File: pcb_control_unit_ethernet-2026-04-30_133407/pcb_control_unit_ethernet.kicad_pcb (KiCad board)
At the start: 4 copper layers, 188 x 65 mm, 274 parts, among them J1 STDC14, J17 STEP1, J18 STEP2, J2 Micro_SD_Card_Det1, J23 Weight, J3 INB, J30 Valve, J4 DC IN, J5 USB STM32, J6 USB STM32, Q1 IRLML6344, Q2 IRLML6344, Q3 IRLML6344, Q4 MMBT4403, Q5 IRLML6344, Q6 IRLML6344, SW1 Reset, SW2 Boot, U1 STM32H563VITx, U10 SIT3051TK, U11 74AHCT125, U12 TPS54202DDC, U16 24LC512, U2 LAN8742A, U4 TPS54202DDC, U5 AMS1117-3.3, U6 INA226, U7 TMC2209, U8 TMC2209, U9 HX711, X1 MT3608, Y1 25MHz, Y2 25MHz

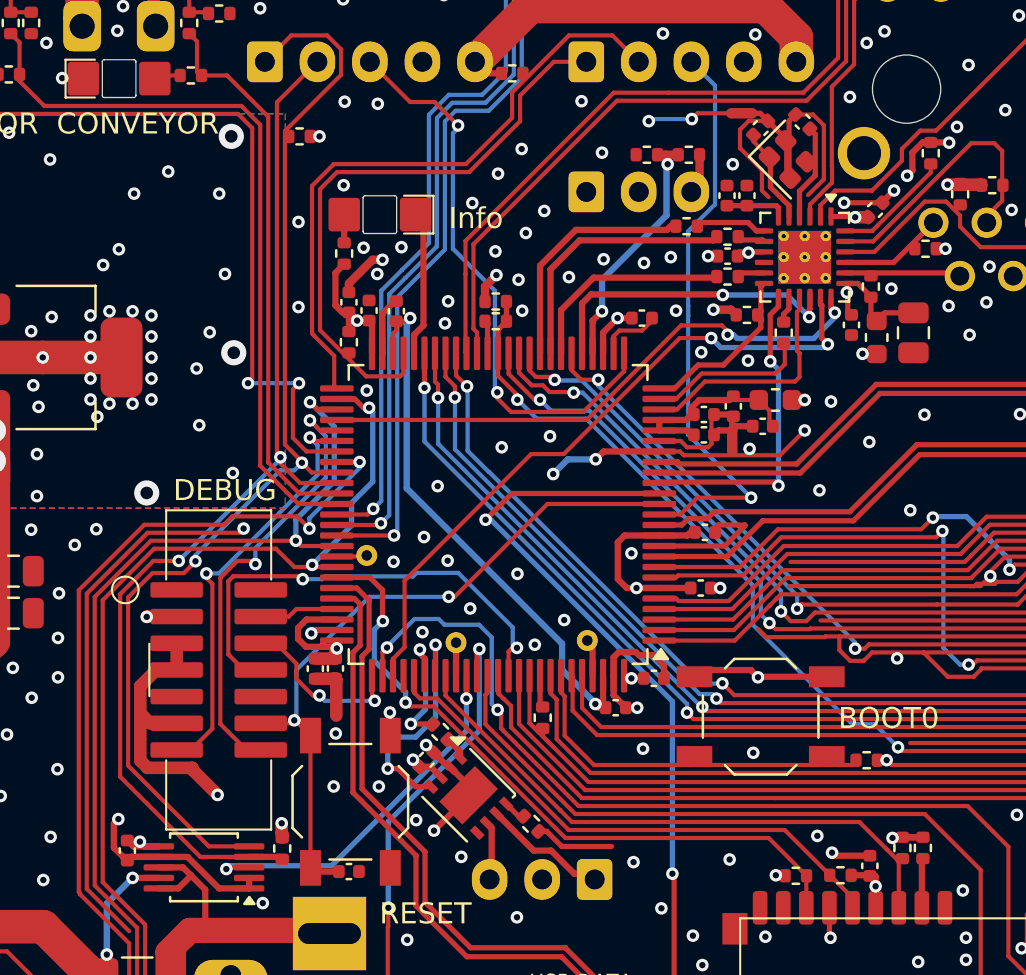
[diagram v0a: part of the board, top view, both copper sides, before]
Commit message: pcb_control_unit_ethercat as ordered @ JLCPCB
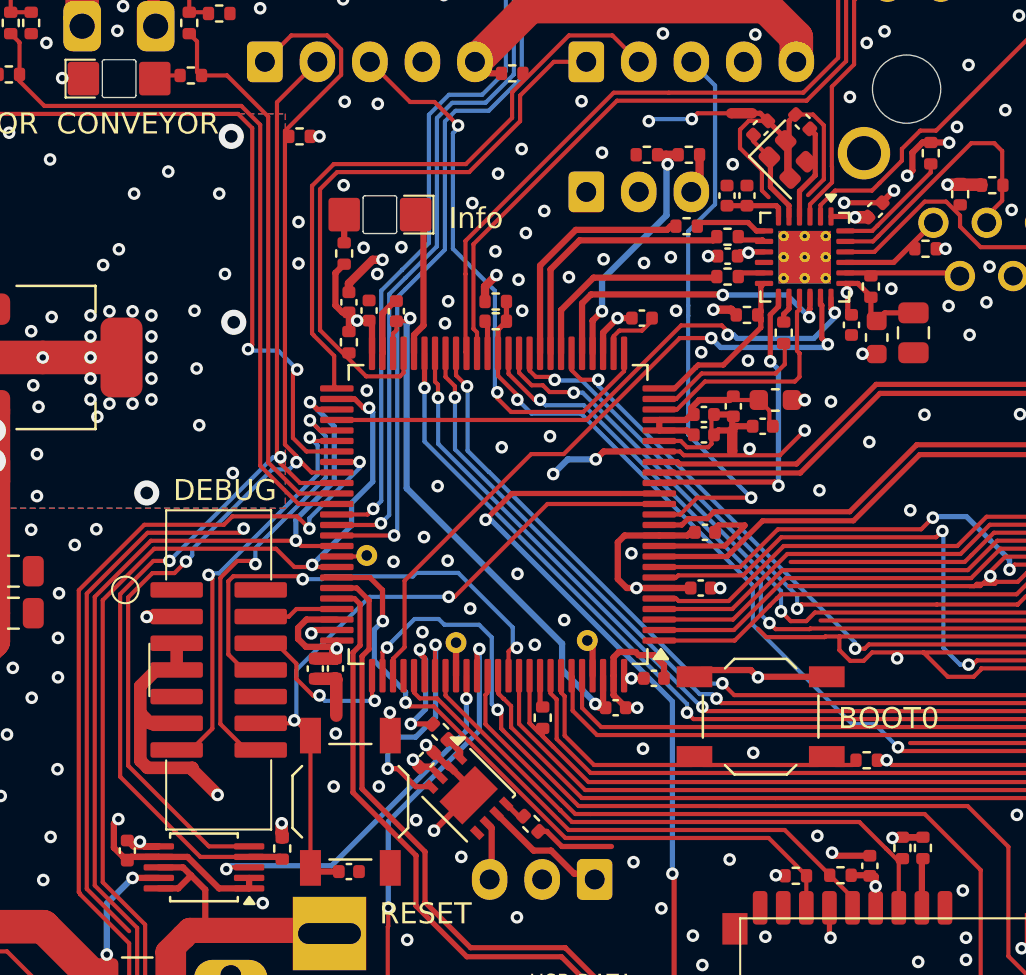
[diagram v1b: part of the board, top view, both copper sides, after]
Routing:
- net +3V3: track 527.0 -> 526.1 mm
- net VALVE1: track 42.5 -> 41.8 mm
